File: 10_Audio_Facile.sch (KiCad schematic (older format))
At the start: 20 parts, among them J1 Conn_01x01, J2 Conn_01x01, J3 Conn_01x01, J4 Conn_01x01, J5 Conn_01x01, J6 Conn_01x01, U1 PAM8302AAS

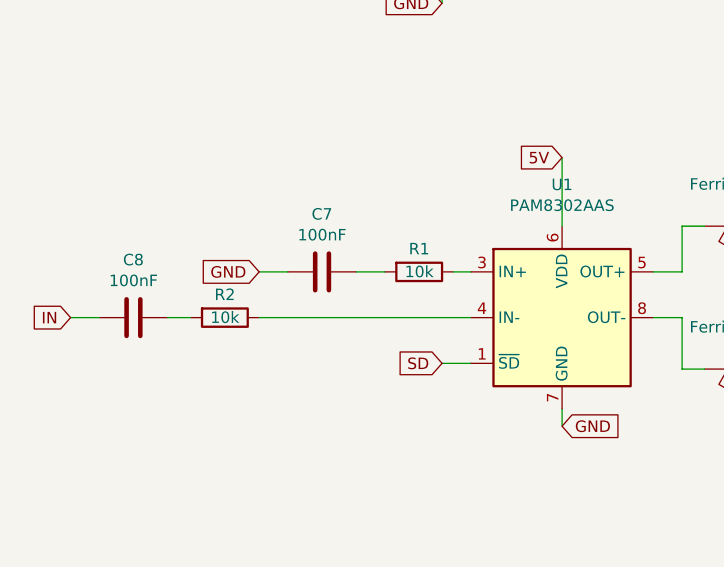
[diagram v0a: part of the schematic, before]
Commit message: suppression résistances entrées
schéma et routage à jour
raf: optimisation taille de la carte
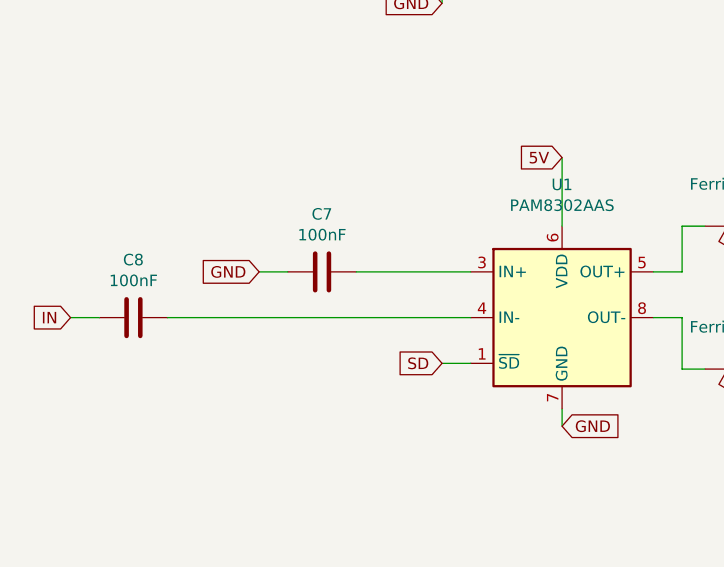
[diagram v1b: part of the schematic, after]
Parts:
- removed R1, R2: 10k, Resistor_SMD:R_0603_1608Metric_Pad1.05x0.95mm_HandSolder, symbol Device:R
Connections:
- net at U1.3 (IN+): now also C7.1
- net at U1.4 (IN-): now also C8.1
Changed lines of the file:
@@
 	4175 3125 4175 3425
-$Comp
-L Device:R R?
-U 1 1 5FE62915
-P 3550 3625
-AR Path="/5FC6D1B4/5FE62915" Ref="R?"  Part="1"
-AR Path="/5FC6C772/5FE62915" Ref="R?"  Part="1"
-AR Path="/5FE62915" Ref="R1"  Part="1"
-F 0 "R1" V 3450 3625 50  0000 C CNN
-F 1 "10k" V 3550 3625 50  0000 C CNN
-F 2 "Resistor_SMD:R_0603_1608Metric_Pad1.05x0.95mm_HandSolder" V 3480 3625 50  0001 C CNN
-F 3 " C25804" H 3550 3625 50  0001 C CNN
-	1    3550 3625
-	0    1    1    0
-$EndComp
-$Comp
-L Device:R R?
-U 1 1 5FE62EEF
-P 2700 3825
-AR Path="/5FC6D1B4/5FE62EEF" Ref="R?"  Part="1"
-AR Path="/5FC6C772/5FE62EEF" Ref="R?"  Part="1"
-AR Path="/5FE62EEF" Ref="R2"  Part="1"
-F 0 "R2" V 2600 3825 50  0000 C CNN
-F 1 "10k" V 2700 3825 50  0000 C CNN
-F 2 "Resistor_SMD:R_0603_1608Metric_Pad1.05x0.95mm_HandSolder" V 2630 3825 50  0001 C CNN
-F 3 " C25804" H 2700 3825 50  0001 C CNN
-	1    2700 3825
-	0    1    1    0
-$EndComp
-Wire Wire Line
-	3700 3625 3775 3625
 $Comp
 L Device:C C7
@@
 	0    1    1    0
 $EndComp
-Wire Wire Line
-	2450 3825 2550 3825
-Wire Wire Line
-	3275 3625 3400 3625
 Text GLabel 2850 3625 0    50   Input ~ 0
 GND
@@
 Text Notes 8675 2550 0    50   ~ 0
 PAM8302\nC112137\nPackage_SO:SOP-8_3.9x4.9mm_P1.27mm\n\nOU\n\nC113367\nPackage_SO:MSOP-8_3x3mm_P0.65mm
-Wire Wire Line
-	2850 3825 3775 3825
 $Bitmap
 Pos 9275 4400
@@
 Wire Wire Line
 	3650 2300 3650 2450
+Wire Wire Line
+	3275 3625 3775 3625
+Wire Wire Line
+	2450 3825 3775 3825
 $EndSCHEMATC

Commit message: maj split librairies
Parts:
- J1, J2, J3, J4, J5, J6: footprint Chimere:Castellated_conn -> Chimere_mods:Castellated_conn
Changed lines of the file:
@@
 F 0 "J1" H 4380 5117 50  0000 L CNN
 F 1 "Conn_01x01" H 4380 5026 50  0000 L CNN
-F 2 "Chimere:Castellated_conn" H 4300 5075 50  0001 C CNN
+F 2 "Chimere_mods:Castellated_conn" H 4300 5075 50  0001 C CNN
 F 3 "~" H 4300 5075 50  0001 C CNN
 	1    4300 5075
@@
 F 0 "J3" H 4380 5467 50  0000 L CNN
 F 1 "Conn_01x01" H 4380 5376 50  0000 L CNN
-F 2 "Chimere:Castellated_conn" H 4300 5425 50  0001 C CNN
+F 2 "Chimere_mods:Castellated_conn" H 4300 5425 50  0001 C CNN
 F 3 "~" H 4300 5425 50  0001 C CNN
 	1    4300 5425
@@
 F 0 "J4" H 4380 5642 50  0000 L CNN
 F 1 "Conn_01x01" H 4380 5551 50  0000 L CNN
-F 2 "Chimere:Castellated_conn" H 4300 5600 50  0001 C CNN
+F 2 "Chimere_mods:Castellated_conn" H 4300 5600 50  0001 C CNN
 F 3 "~" H 4300 5600 50  0001 C CNN
 	1    4300 5600
@@
 F 0 "J5" H 4380 5817 50  0000 L CNN
 F 1 "Conn_01x01" H 4380 5726 50  0000 L CNN
-F 2 "Chimere:Castellated_conn" H 4300 5775 50  0001 C CNN
+F 2 "Chimere_mods:Castellated_conn" H 4300 5775 50  0001 C CNN
 F 3 "~" H 4300 5775 50  0001 C CNN
 	1    4300 5775
@@
 F 0 "J6" H 4380 5992 50  0000 L CNN
 F 1 "Conn_01x01" H 4380 5901 50  0000 L CNN
-F 2 "Chimere:Castellated_conn" H 4300 5950 50  0001 C CNN
+F 2 "Chimere_mods:Castellated_conn" H 4300 5950 50  0001 C CNN
 F 3 "~" H 4300 5950 50  0001 C CNN
 	1    4300 5950
@@
 F 0 "J2" H 4380 5292 50  0000 L CNN
 F 1 "Conn_01x01" H 4380 5201 50  0000 L CNN
-F 2 "Chimere:Castellated_conn" H 4300 5250 50  0001 C CNN
+F 2 "Chimere_mods:Castellated_conn" H 4300 5250 50  0001 C CNN
 F 3 "~" H 4300 5250 50  0001 C CNN
 	1    4300 5250
